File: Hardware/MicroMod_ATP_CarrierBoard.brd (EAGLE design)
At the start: 101.6 x 58.4 mm, 153 parts, among them IC3 LM1117, J19 QWIIC_RIGHT_ANGLE, J2 JTAG, J20 QWIIC_RIGHT_ANGLE, J21 1X04_SMD_STRAIGHT_COMBO, J23 1X04_SMD_STRAIGHT_COMBO, J26 POWER_JACKTOE, J6 MICROMOD-2222-C, J8 1X04_SMD_STRAIGHT_COMBO, Q1 2.5A/30V/105mΩ, U5 AP7361C-33

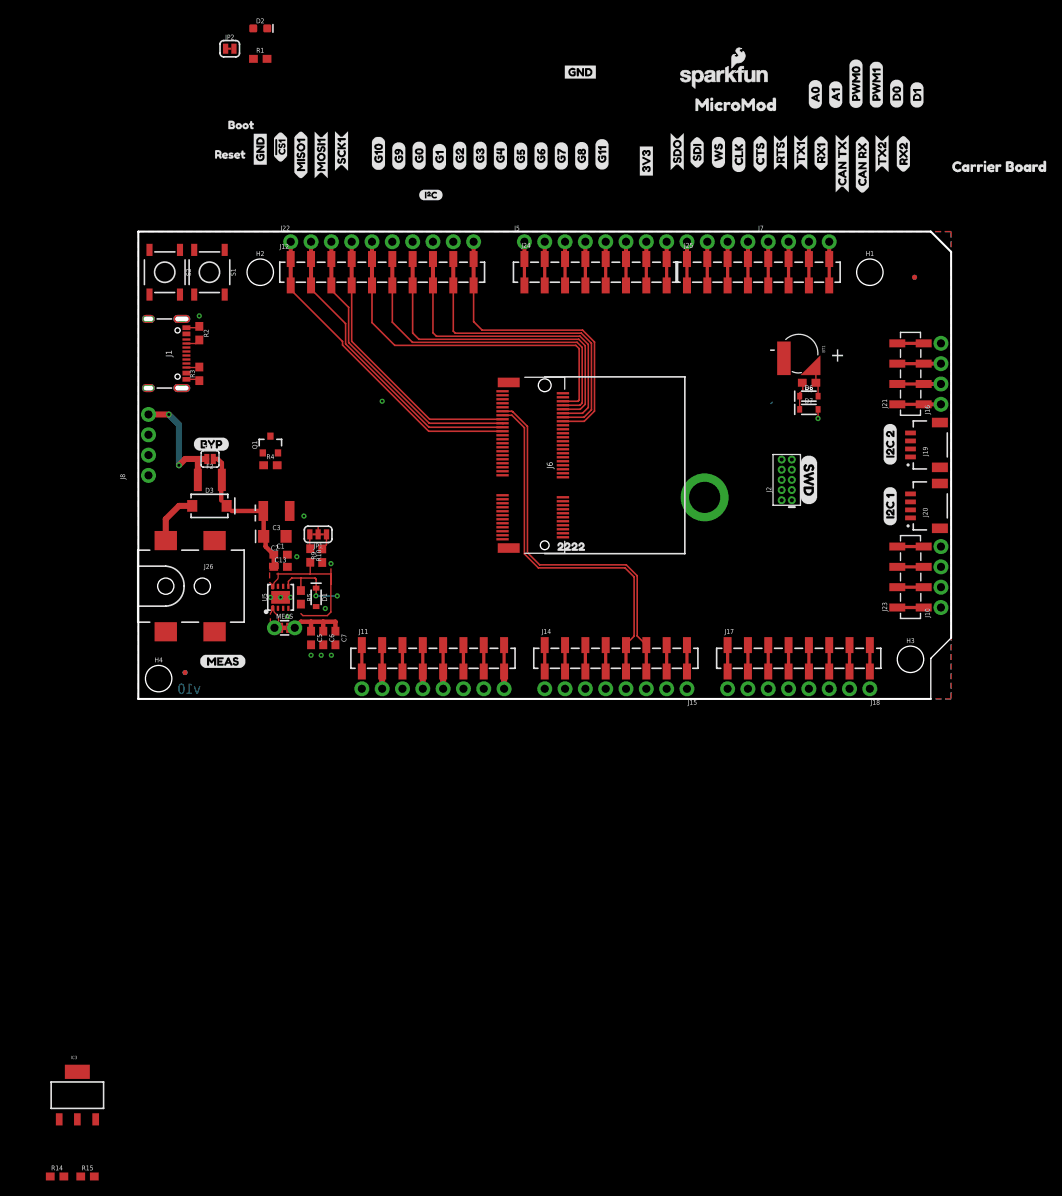
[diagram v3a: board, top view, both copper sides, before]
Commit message: "Reverts" back to a time when barrel jack did not exist
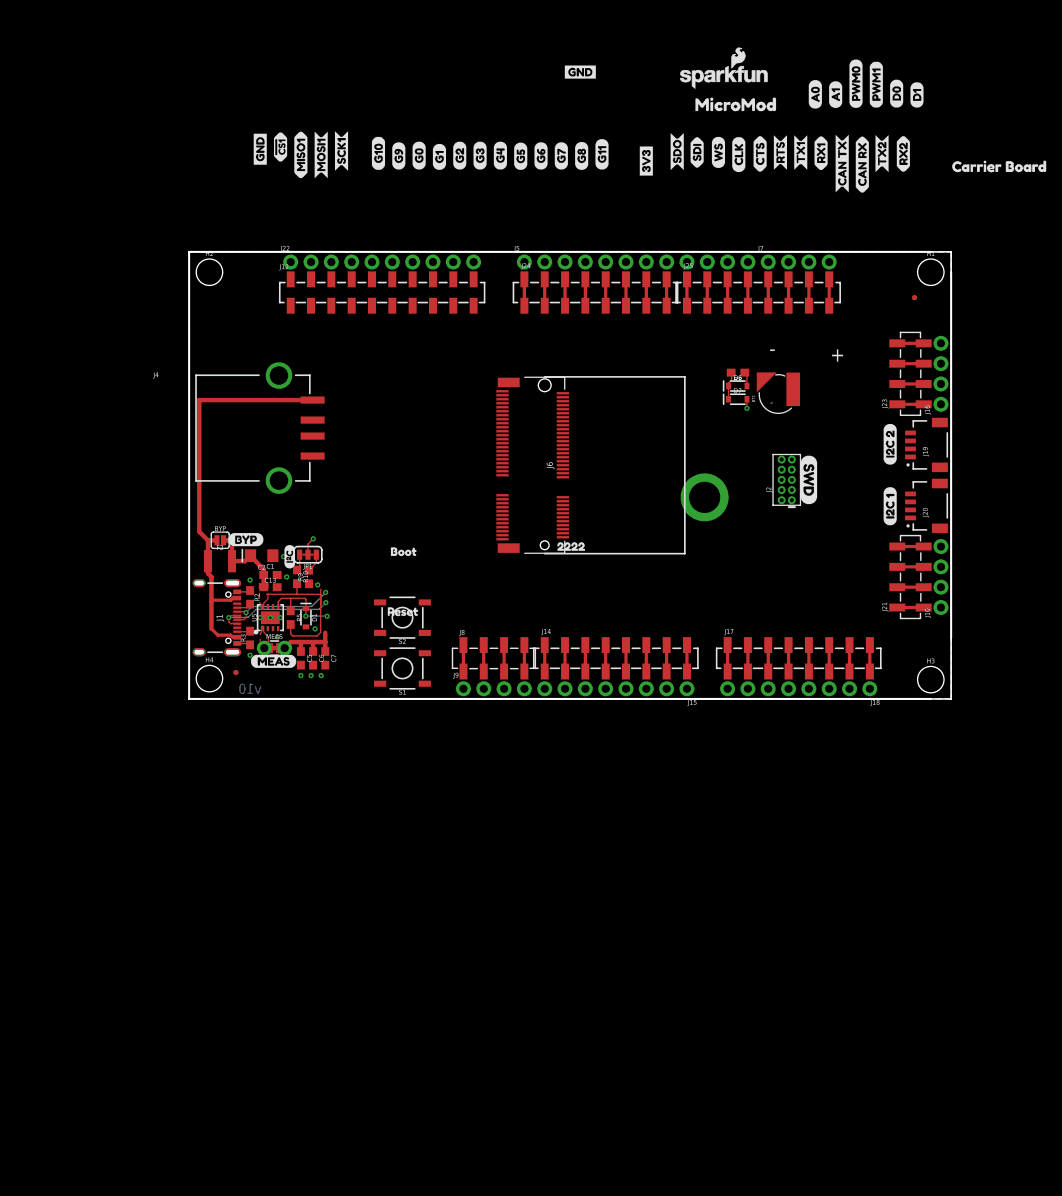
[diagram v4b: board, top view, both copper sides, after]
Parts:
- removed C3: 47uF, SparkFun-Capacitors:EIA3528
- removed D2: RED, SparkFun-LED:LED-0603
- removed D3: 1A/40V/500mV, SparkFun-DiscreteSemi:SMA-DIODE
- removed IC3: LM1117, Testing:SOT223-ALT1
- removed J11: (no value), SparkFun-Connectors:1X08_SMD_COMBINED
- removed J13: (no value), SparkFun-Connectors:1X08_NO_SILK
- removed J26: POWER_JACKTOE, SparkFun-Connectors:POWER_JACK_SMD_OVERPASTE_TOE
- removed JP2: JUMPER-SMT_2_NC_TRACE_SILK, SparkFun-Jumpers:SMT-JUMPER_2_NC_TRACE_SILK
- removed Q1: 2.5A/30V/105mΩ, SparkFun-DiscreteSemi:SOT23-3
- removed R1: 1k, SparkFun-Resistors:0603
- removed R14: 715, SparkFun-Resistors:0603
- removed R15: 240, SparkFun-Resistors:0603
- removed R4: 10k, SparkFun-Resistors:0603
- added J4: USB_A_SMT_FEMALE, SparkFun-Connectors:USB-A-S-SILK-FEMALE
- added J9: (no value), SparkFun-Connectors:1X04_NO_SILK
- D1: device SparkFun-DiscreteSemi:SOD-323@1 -> SparkFun-DiscreteSemi:SOD-323
- J8: device SparkFun-Connectors:1X04_NO_SILK -> SparkFun-Connectors:1X04_SMD_VERTICAL_COMBO
- moved U$2 61.1 mm to (30.2, 10.9)
- moved U$19 57.1 mm to (30.6, 18.4)
- moved S1 55.1 mm to (33.0, 3.81), turned to 180 degrees
- moved S2 52.4 mm to (33.0, 10.2), turned to 180 degrees
- moved U$42 49.4 mm to (18.9, 16.3), turned to 90 degrees
- moved J8 45.5 mm to (40.6, 5.08), turned to 0 degrees
- moved R3 33.6 mm to (14.0, 7.62)
- moved J1 33.6 mm to (12.7, 10.2)
- moved R2 33.6 mm to (14.0, 12.7)
- moved J21 25.4 mm to (96.5, 11.4)
- moved J23 25.4 mm to (96.5, 36.8)
- moved U$27 12.7 mm to (11.2, 19.9)
- moved BYP 10.2 mm to (10.2, 19.8)
- moved F2 10.2 mm to (10.2, 17.2)
- moved R8 8.98 mm to (75.0, 40.8)
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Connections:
- net ADC_N renamed G9/ADC_N
- net ADC_P renamed G10/ADC_P
- removed net 5V: C1.1, C13.1, C2.+, IC3.2, IC3.4, J11.4, J11.4@2, J13.5, Q1.2, R15.2, R4.2, R5.2, U5.8
- removed net INSERT: J26.P$4, Q1.1, R4.1
- removed net N$1: D2.A, R1.1
- removed net N$15: IC3.1, R14.2, R15.1
- removed net N$4: D2.C, JP2.2
- removed net PWRIN: D3.A, J26.VIN0
- removed net SHIELD: J1.SHLD1, J1.SHLD2, J1.SHLD3, J1.SHLD4
- removed net VDD: J11.2, J11.2@2, J11.5, J11.5@2, J13.4, J13.7
- net !CS1: now also J12.4A, J12.4B, J22.4; no longer J12.1A, J12.1B, J22.1
- net !RESET: no longer J11.3, J11.3@2, J13.6
- net 3.3V: no longer R1.2
- net GND: now also J4.GND, J4.SHLD1, J4.SHLD2; no longer C3.C, J11.6, J11.6@2, J11.7, J11.7@2, J13.2, J13.3, J26.GND, J8.1, JP2.1, R14.1
- net MISO1: now also J12.3A, J12.3B, J22.3; no longer J12.4A, J12.4B, J22.4
- net MOSI1: now also J12.2A, J12.2B, J22.2; no longer J12.3A, J12.3B, J22.3
- net SCLK1: now also J12.1A, J12.1B, J22.1; no longer J12.2A, J12.2B, J22.2
- net SPI_MOSI: now also J12.10A, J12.10B, J3.6; no longer J12.9A, J12.9B, J3.5
- net SPI_SCK: now also J12.9A, J12.9B, J3.5; no longer J12.10A, J12.10B, J3.6
- net USBHOST_N: now also J4.D-; no longer J8.3
- net USBHOST_P: now also J4.D+; no longer J8.2
- net VIN: now also C1.1, C13.1, C2.+, R5.2, U5.8; no longer C3.A, D3.C, IC3.3, J11.8, J11.8@2, J13.1
- net V_USB: now also J4.VBUS; no longer J8.4, Q1.3
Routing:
- net SD_!CS!: track 45.9 -> 0.00 mm
- net G9/ADC_N: track 43.7 -> 0.00 mm
- net G10/ADC_P: track 43.0 -> 0.00 mm
- net SD_DAT2: track 42.5 -> 0.00 mm
- net SD_DAT1: track 41.8 -> 0.00 mm
- net SPI_MISO: track 40.6 -> 0.00 mm
- net !CS1: track 40.1 -> 0.00 mm
- net SPI_SCK: track 39.6 -> 0.00 mm
- net SPI_MOSI: track 39.2 -> 0.00 mm
- net SCLK1: track 38.5 -> 0.00 mm
- net MOSI1: track 37.0 -> 0.00 mm
- net V_USB: track 15.9 -> 51.6 mm, vias 2 -> 0
- net MISO1: track 35.3 -> 0.00 mm
- net USB_P: track 0.00 -> 15.7 mm, vias 0 -> 2
- net USB_N: track 0.00 -> 14.0 mm, vias 0 -> 2
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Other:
- board size 101.6 x 58.4 mm -> 95.2 x 55.9 mm

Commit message: Shrinks board, adds routing
* board is now 2 x 3 roughly
* Added a longer header for MCLK and GND -> went from 10-12 pin
*  Routed SPI, QSPI, and I2S
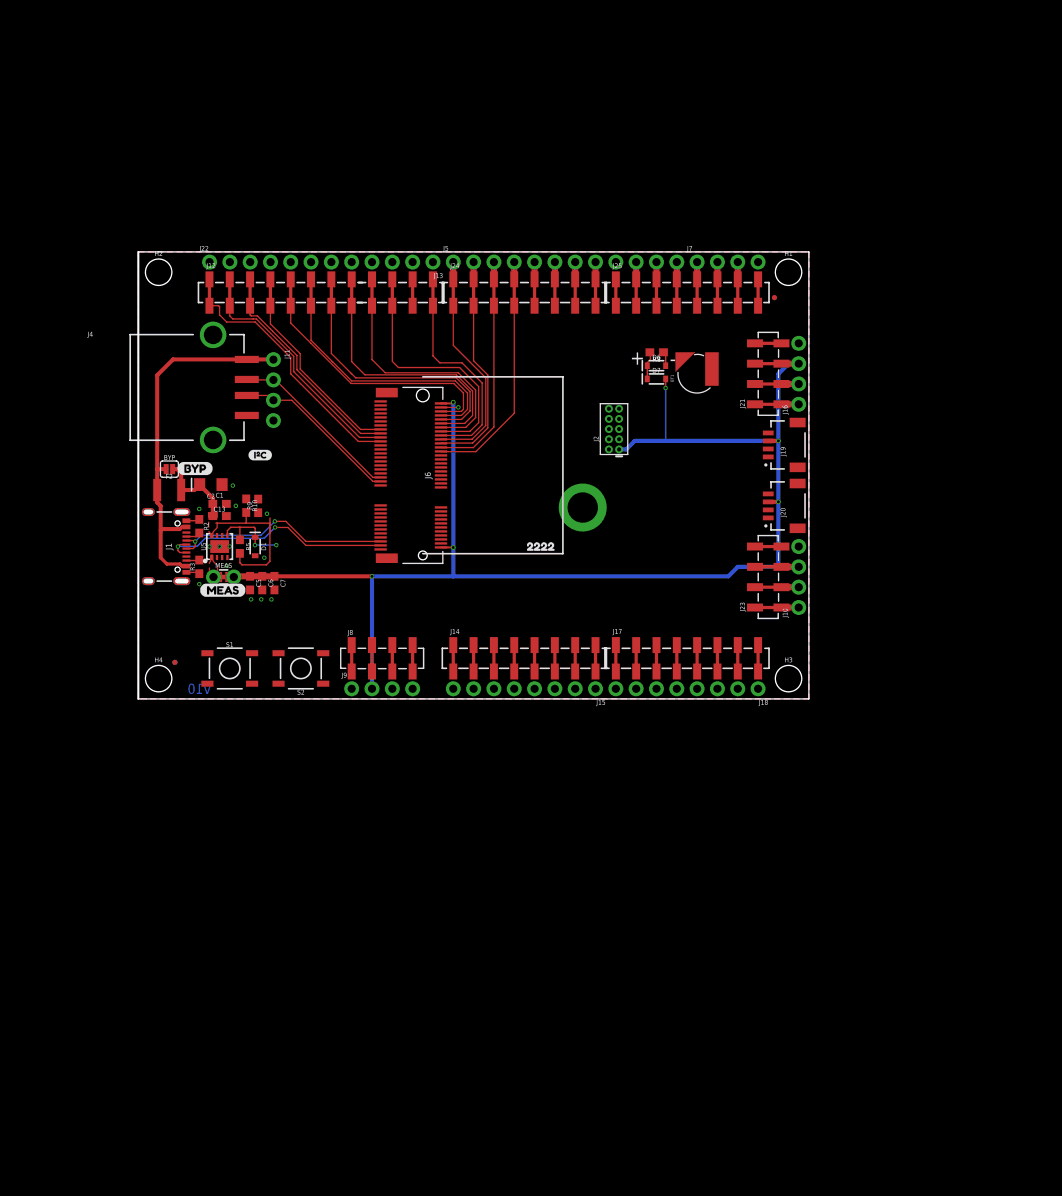
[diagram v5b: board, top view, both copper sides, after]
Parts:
- removed J3: (no value), SparkFun-Connectors:1X06_NO_SILK
- removed JP1: JUMPER-SMT_3_2-NC_TRACE_SILK, SparkFun-Jumpers:SMT-JUMPER_3_2-NC_TRACE_SILK
- removed LOGO1: SFE_LOGO_NAME_FLAME.1_INCH, SparkFun-Aesthetics:SFE_LOGO_NAME_FLAME_.1
- removed U$1, U$89: (no value), Bus Labels:G00
- removed U$10, U$75: (no value), SPI1:MISO10
- removed U$11, U$86: (no value), Bus Labels:G33
- removed U$12, U$13: (no value), buzzard_labels (12):D13
- removed U$14, U$16: (no value), buzzard_labels (12):D02
- removed U$15, U$61: (no value), buzzard_labels (10):PWM10
- removed U$17, U$85: (no value), Bus Labels:G44
- removed U$18, U$84: (no value), Bus Labels:G55
- removed U$19: (no value), buzzard_labels (10):BOOT2
- removed U$2: (no value), buzzard_labels (9):RESET3
- removed U$20, U$83: (no value), Bus Labels:G66
- removed U$22, U$82: (no value), Bus Labels:G77
- removed U$23, U$26: (no value), SparkFun-Buzzard:3V3_P
- removed U$24: (no value), buzzard_labels (11):MICROMOD0
- removed U$25, U$29: (no value), buzzard_labels (6):RX10
- removed U$3, U$88: (no value), Bus Labels:G11
- removed U$30, U$80: (no value), Bus Labels:G118
- removed U$31, U$41: (no value), buzzard_labels (6):TX13
- removed U$32, U$81: (no value), Bus Labels:G811
- removed U$33: (no value), Bus Labels:G1010
- removed U$34, U$48: (no value), Top PTH:CAN_RX2
- removed U$36, U$54: (no value), Top PTH:CAN_TX3
- removed U$37, U$62: (no value), Top PTH:CLK3
- removed U$38, U$63: (no value), Top PTH:SDI1
- removed U$39, U$65: (no value), Top PTH:SDO0
- removed U$4, U$87: (no value), Bus Labels:G22
- removed U$40, U$66: (no value), Top PTH:WS2
- removed U$43, U$44: (no value), buzzard_labels (12):A00
- removed U$45: (no value), Carrier Board:CARRIER_BOARD0
- removed U$47: (no value), SWD:SWD0
- removed U$49, U$76: (no value), SPI1:MOSI11
- removed U$50, U$77: (no value), SPI1:SCK12
- removed U$51, U$78: (no value), SERIAL2:CTS0
- removed U$52, U$79: (no value), SERIAL2:RTS1
- removed U$53, U$6, U$73: (no value), SparkFun-Buzzard:GND_P
- removed U$56: (no value), G9:G90
- removed U$57, U$58: (no value), buzzard_labels (1):A10
- removed U$59, U$60: (no value), buzzard_labels (1):PWM01
- removed U$67: (no value), Extra I2C Lables:I2C_10
- removed U$68: (no value), Extra I2C Lables:I2C_21
- removed U$69, U$70: (no value), SERIAL2:RX23
- removed U$7: (no value), CAM_ADC:ADC_D##CAM_HSYNC0
- removed U$71, U$72: (no value), SERIAL2:TX22
- removed U$74, U$9: (no value), SPI1:#CS13
- removed U$8: (no value), CAM_ADC:ADC_D##CAM_VSYNC1
- added J11: (no value), SparkFun-Connectors:1X04_NO_SILK
- added J13: (no value), SparkFun-Connectors:1X08_NO_SILK
- J12: device SparkFun-Connectors:1X10_SMD_COMBINED -> SparkFun-Connectors:1X12_SMD_COMBINED
- moved J21 31.0 mm to (78.7, 36.8)
- moved J23 31.0 mm to (78.7, 11.4)
- moved FRAME1 26.9 mm to (20.6, -15.7)
- moved J2 22.5 mm to (59.5, 33.7)
- moved S1 21.6 mm to (11.4, 3.81), turned to 0 degrees
- moved H3 17.8 mm to (81.3, 2.54)
- moved H1 17.8 mm to (81.3, 53.3)
- moved J10 17.8 mm to (82.5, 11.4)
- moved J16 17.8 mm to (82.5, 36.8)
- moved J19 17.8 mm to (78.7, 31.8)
- moved J20 17.8 mm to (78.7, 24.1)
- moved FD2 17.5 mm to (79.5, 50.2)
- moved FD4 17.5 mm to (79.5, 50.2)
- moved H5 15.3 mm to (55.5, 23.9)
- moved J6 15.3 mm to (35.6, 27.9)
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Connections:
- removed net N$2: JP1.3, R10.1
- removed net N$3: JP1.1, R9.2
- new net !RESET!: J8.3, J8.3-2, J9.3
- net !CS1: now also J12.1, J12.1@2, J22.1; no longer J12.4A, J12.4B, J22.4
- net 3.3V: now also J8.2, J8.2-2, J9.2
- net GND: now also J11.4, J12.11, J12.11@2, J13.2, J8.4, J8.4-2, J9.4
- net MCLK: now also J12.12, J12.12@2, J13.1
- net MISO1: now also J12.4, J12.4@2, J22.4; no longer J12.3A, J12.3B, J22.3
- net MOSI1: now also J12.3, J12.3@2, J22.3; no longer J12.2A, J12.2B, J22.2
- net SCLK1: now also J12.2, J12.2@2, J22.2; no longer J12.1A, J12.1B, J22.1
- net SD_!CS!: now also J12.5, J12.5@2, J13.8; no longer J12.5A, J12.5B, J3.1
- net SD_DAT1: now also J12.7, J12.7@2, J13.6; no longer J12.7A, J12.7B, J3.3
- net SD_DAT2: now also J12.6, J12.6@2, J13.7; no longer J12.6A, J12.6B, J3.2
- net SPI_MISO: now also J12.8, J12.8@2, J13.5; no longer J12.8A, J12.8B, J3.4
- net SPI_MOSI: now also J12.9, J12.9@2, J13.4; no longer J12.10A, J12.10B, J3.6
- net SPI_SCK: now also J12.10, J12.10@2, J13.3; no longer J12.9A, J12.9B, J3.5
- net USBHOST_N: now also J11.2
- net USBHOST_P: now also J11.3
- net VIN: now also J8.1, J8.1-2, J9.1
- net VIN/3: now also R10.1, R9.2; no longer JP1.2
- net V_USB: now also J11.1
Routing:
- net 3.3V: track 12.2 -> 173.1 mm, vias 1 -> 6
- net SD_DAT2: track 0.00 -> 32.3 mm
- net SD_DAT1: track 0.00 -> 31.8 mm
- net SD_!CS!: track 0.00 -> 31.4 mm
- net SPI_MISO: track 0.00 -> 31.0 mm
- net !CS1: track 0.00 -> 30.2 mm
- net SPI_MOSI: track 0.00 -> 29.5 mm
- net SPI_SCK: track 0.00 -> 28.7 mm
- net SCLK1: track 0.00 -> 27.5 mm
- net I2S_CLK: track 0.00 -> 26.5 mm
- net I2S_SDO: track 0.00 -> 24.8 mm
- net MCLK: track 0.00 -> 24.7 mm
- net I2S_WS: track 0.00 -> 24.7 mm
- net MOSI1: track 0.00 -> 24.6 mm
- net I2S_SDI: track 0.00 -> 24.5 mm
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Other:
- board size 95.2 x 55.9 mm -> 83.8 x 55.9 mm

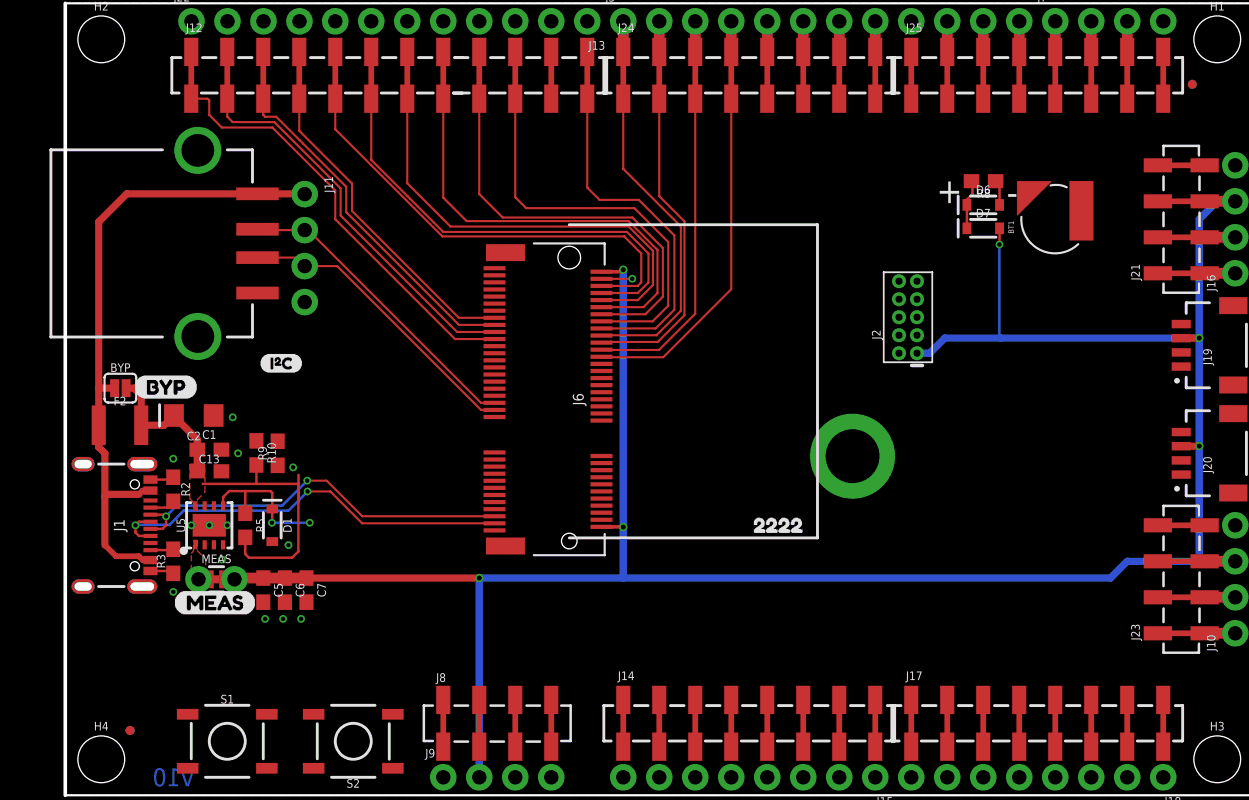
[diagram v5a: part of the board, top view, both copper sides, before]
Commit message: Routes the Analog and RX2 traces
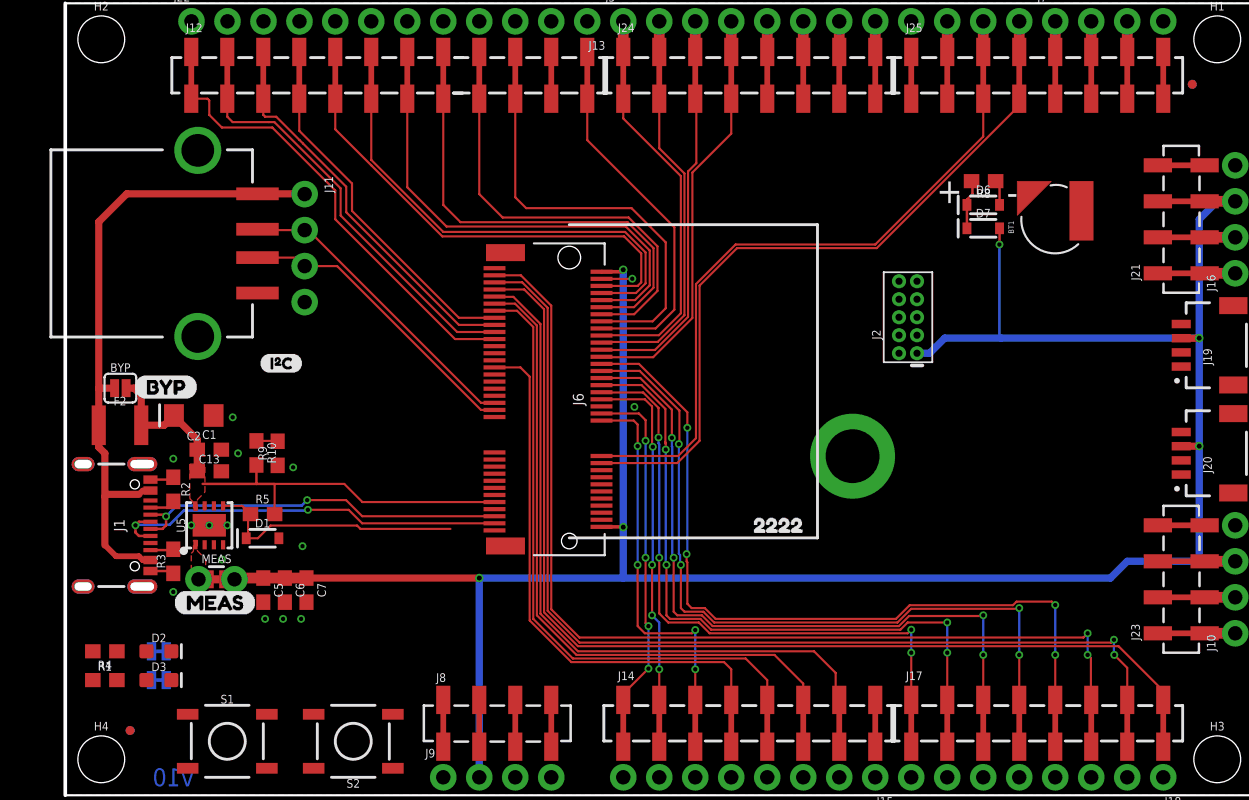
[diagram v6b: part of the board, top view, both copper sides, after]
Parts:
- added D2, D3: RED, SparkFun-LED:LED-0603
- added JP1, JP2: JUMPER-SMT_2_NC_TRACE_SILK, SparkFun-Jumpers:SMT-JUMPER_2_NC_TRACE_SILK
- added R1, R4: 1k, SparkFun-Resistors:0603
- moved R5 1.45 mm to (13.9, 19.8), turned to 0 degrees
- moved LOGO3 1.27 mm to (3.81, 10.2)
- moved D1 1.14 mm to (13.9, 18.1), turned to 0 degrees
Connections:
- new net N$1: D2.A, R1.1
- new net N$2: D3.A, R4.1
- new net N$3: D2.C, JP1.1
- new net N$4: D3.C, JP2.1
- net 3.3V: now also R1.2
- net GND: now also JP1.2, JP2.2
- net VIN: now also R4.2
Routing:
- net G6: track 0.00 -> 72.5 mm, vias 0 -> 2
- net G7: track 0.00 -> 72.1 mm
- net G5: track 0.00 -> 70.3 mm, vias 0 -> 2
- net G4: track 0.00 -> 55.7 mm, vias 0 -> 4
- net G3: track 0.00 -> 52.9 mm, vias 0 -> 4
- net G2: track 0.00 -> 49.8 mm, vias 0 -> 4
- net G8: track 0.00 -> 49.1 mm
- net G1: track 0.00 -> 46.8 mm, vias 0 -> 4
- net RX2: track 2.16 -> 48.6 mm
- net G9/ADC_N: track 0.00 -> 46.0 mm
- net TX2: track 2.16 -> 47.5 mm
- net G10/ADC_P: track 0.00 -> 43.9 mm
- net G0: track 0.00 -> 43.4 mm, vias 0 -> 4
- net PWM1: track 0.00 -> 38.8 mm
- net PWM0: track 0.00 -> 27.2 mm, vias 0 -> 4
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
